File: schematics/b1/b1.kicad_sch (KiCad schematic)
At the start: 7 parts, among them SW6 SW_SPDT, U1 L7805, U8 AMS1117-3.3

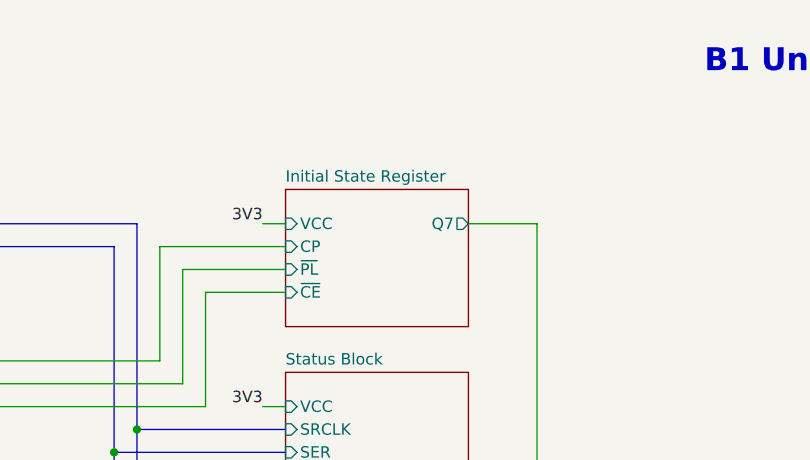
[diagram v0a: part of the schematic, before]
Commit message: Renamed the ISR to the BID Register.
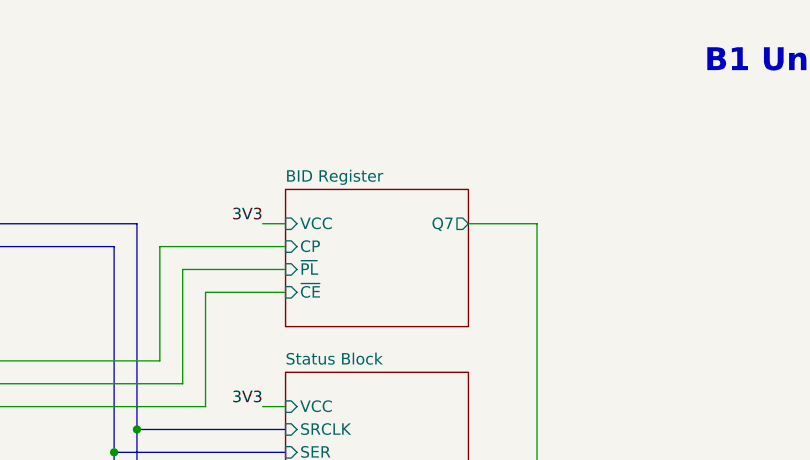
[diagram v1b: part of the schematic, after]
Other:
- sheet Initial State Register renamed BID Register
- sheet BID Register: file initial_state_register.kicad_sch -> bid_register.kicad_sch
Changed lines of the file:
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@@
     (stroke (width 0.1524) (type solid))
     (fill (color 0 0 0 0.0000))
-    (property "Sheetname" "Initial State Register" (at 195.58 31.0384 0)
+    (property "Sheetname" "BID Register" (at 195.58 31.0384 0)
       (effects (font (size 1.27 1.27)) (justify left bottom))
     )
-    (property "Sheetfile" "initial_state_register.kicad_sch" (at 195.58 47.5746 0)
+    (property "Sheetfile" "bid_register.kicad_sch" (at 195.58 47.5746 0)
       (effects (font (size 1.27 1.27)) (justify left top) hide)
     )

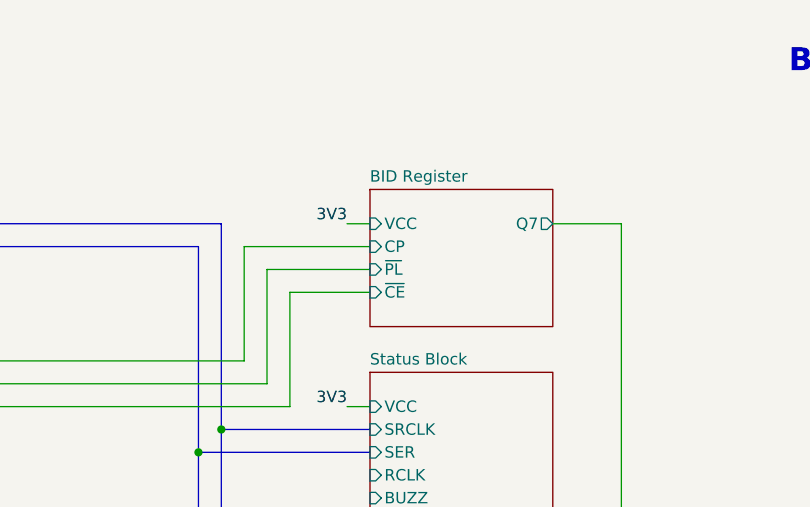
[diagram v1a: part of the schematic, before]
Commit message: Updated the BID register.
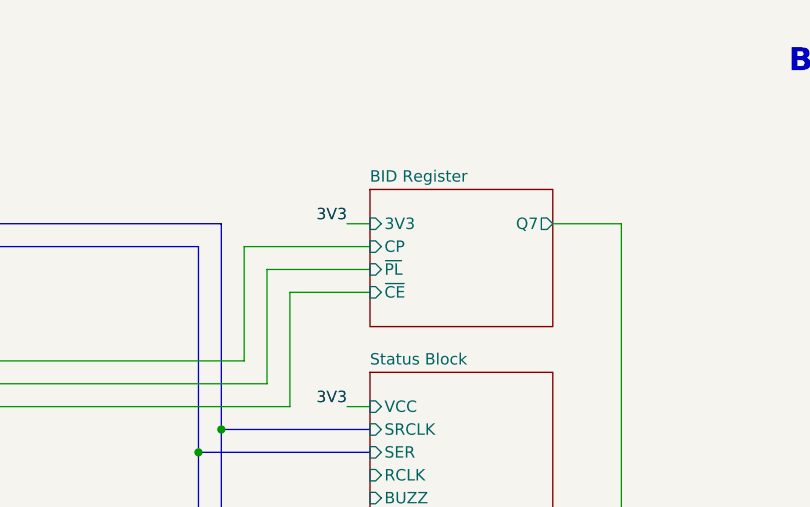
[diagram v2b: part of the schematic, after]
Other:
- sheet BID Register ports: added 3V3; removed VCC
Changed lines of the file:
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@@
       (effects (font (size 1.27 1.27)) (justify right))
-    )
-    (pin "VCC" input (at 195.58 35.56 180)
-      (effects (font (size 1.27 1.27)) (justify left))
     )
     (pin "~{PL}" input (at 195.58 40.64 180)
       (effects (font (size 1.27 1.27)) (justify left))
     )
+    (pin "3V3" input (at 195.58 35.56 180)
+      (effects (font (size 1.27 1.27)) (justify left))
+    )

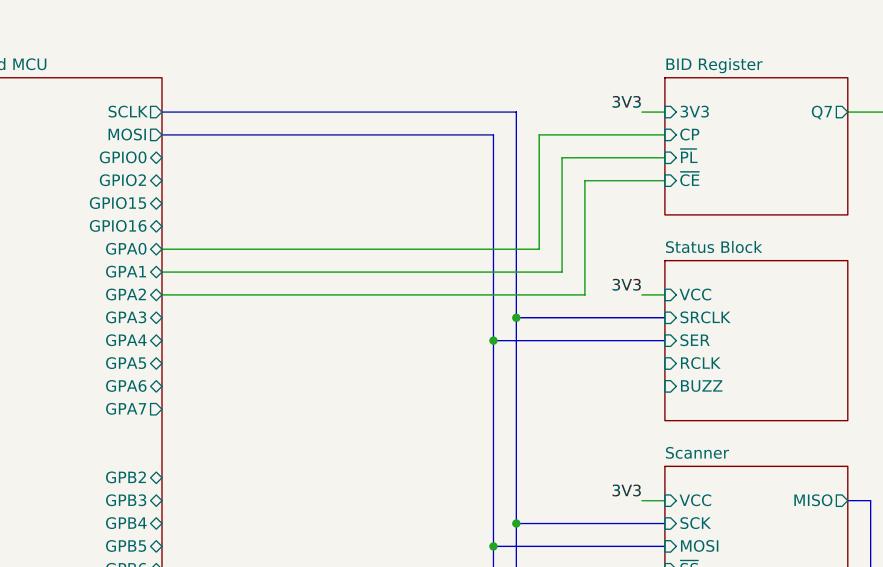
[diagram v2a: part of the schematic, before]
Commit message: Updated status block schematic.
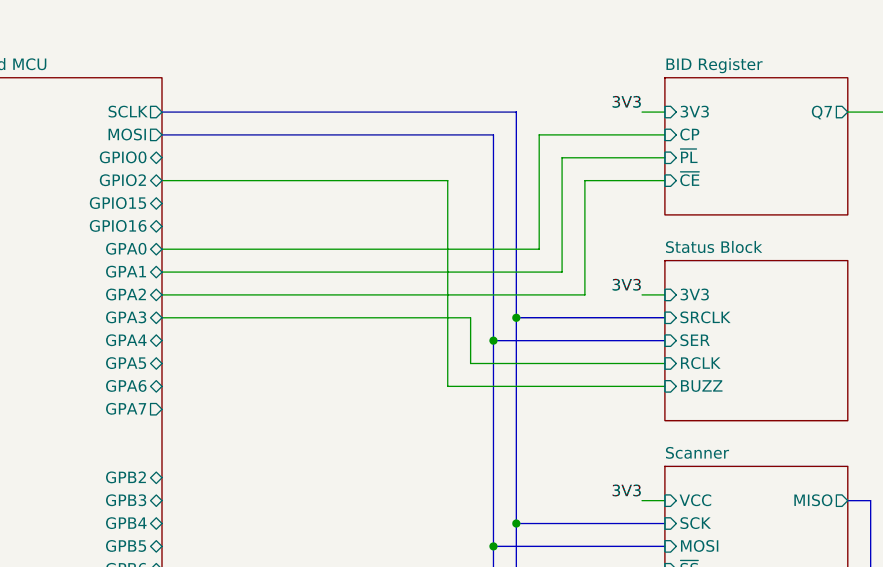
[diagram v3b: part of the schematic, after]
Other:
- sheet Status Block ports: added 3V3; removed VCC
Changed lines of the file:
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@@
+    (stroke (width 0) (type default))
+  )
+  (wire (pts (xy 195.58 63.5) (xy 173.99 63.5))
     (stroke (width 0) (type default))
   )
@@
     (stroke (width 0) (type default))
   )
+  (wire (pts (xy 173.99 63.5) (xy 173.99 58.42))
+    (stroke (width 0) (type default))
+  )
   (wire (pts (xy 184.15 40.64) (xy 184.15 53.34))
     (stroke (width 0) (type default))
@@
     (stroke (width 0) (type default))
   )
+  (wire (pts (xy 171.45 66.04) (xy 171.45 43.18))
+    (stroke (width 0) (type default))
+  )
   (wire (pts (xy 39.37 39.37) (xy 41.91 39.37))
     (stroke (width 0) (type default))
@@
     (stroke (width 0) (type default))
   )
+  (wire (pts (xy 173.99 58.42) (xy 139.7 58.42))
+    (stroke (width 0) (type default))
+  )
   (wire (pts (xy 111.76 35.56) (xy 114.3 35.56))
     (stroke (width 0) (type default))
@@
     (stroke (width 0) (type default))
   )
+  (wire (pts (xy 171.45 43.18) (xy 139.7 43.18))
+    (stroke (width 0) (type default))
+  )
   (bus (pts (xy 195.58 58.42) (xy 179.07 58.42))
     (stroke (width 0) (type default))
@@
   )
   (wire (pts (xy 41.91 69.85) (xy 39.37 69.85))
+    (stroke (width 0) (type default))
+  )
+  (wire (pts (xy 195.58 66.04) (xy 171.45 66.04))
     (stroke (width 0) (type default))
   )
@@
       (effects (font (size 1.27 1.27)) (justify left top) hide)
     )
-    (pin "VCC" input (at 195.58 55.88 180)
-      (effects (font (size 1.27 1.27)) (justify left))
-    )
     (pin "BUZZ" input (at 195.58 66.04 180)
       (effects (font (size 1.27 1.27)) (justify left))
@@
       (effects (font (size 1.27 1.27)) (justify left))
     )
+    (pin "3V3" input (at 195.58 55.88 180)
+      (effects (font (size 1.27 1.27)) (justify left))
+    )

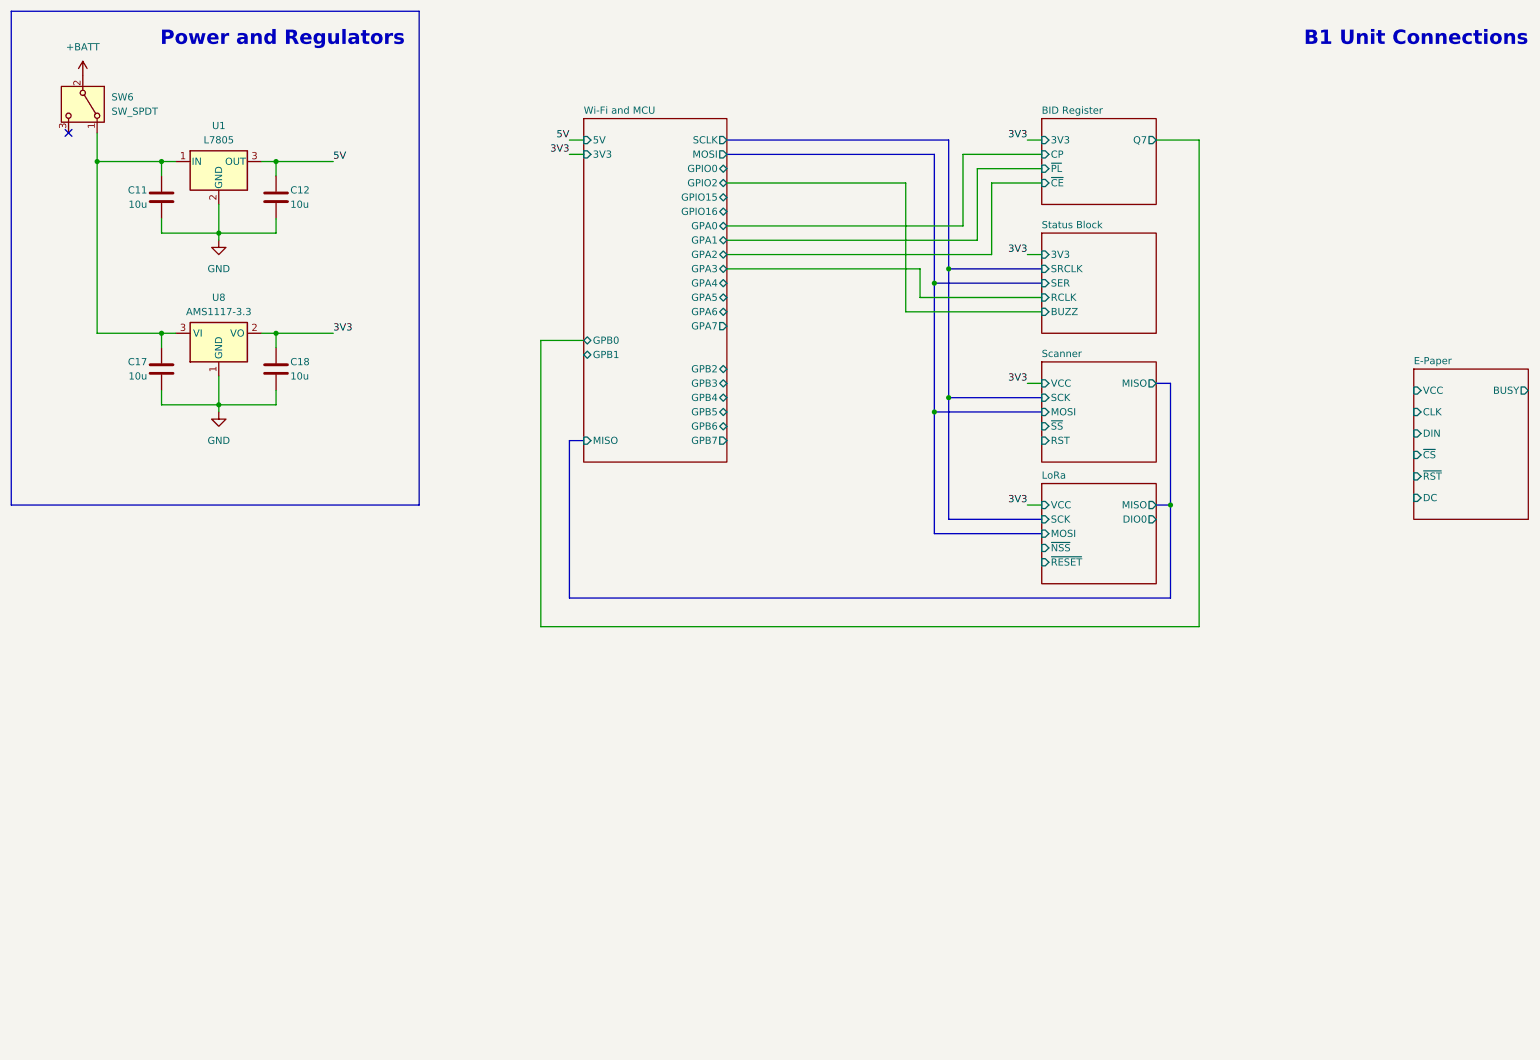
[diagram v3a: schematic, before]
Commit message: Updated RFID scanner wiring.
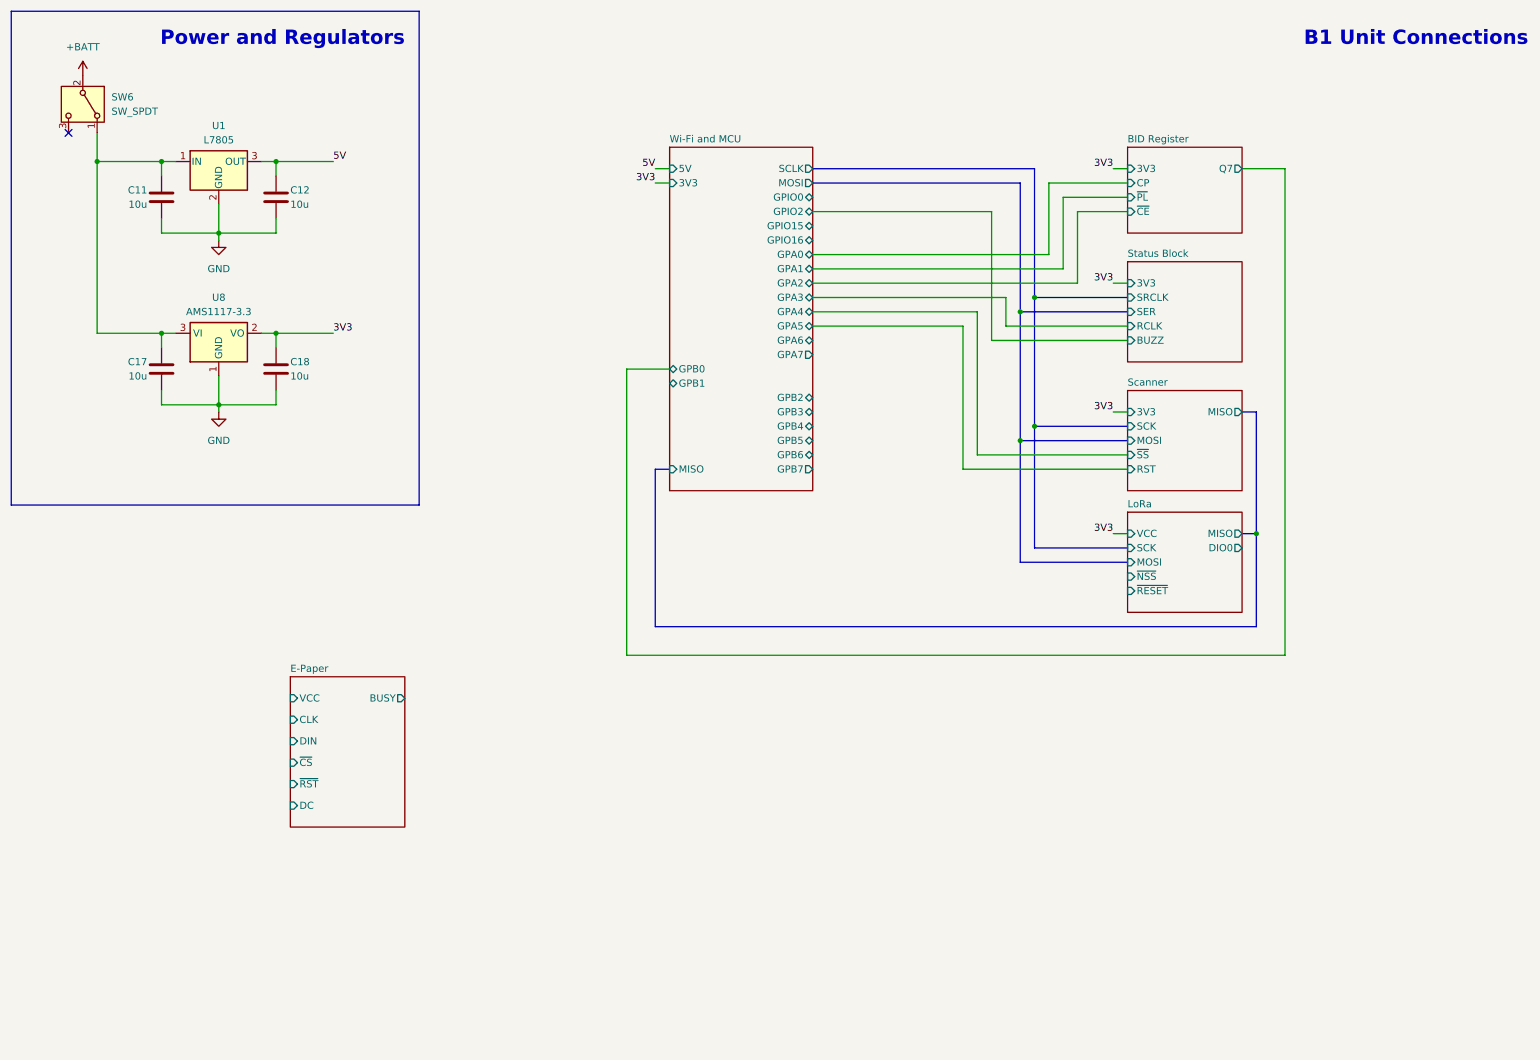
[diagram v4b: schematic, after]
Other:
- sheet Scanner ports: added 3V3; removed VCC

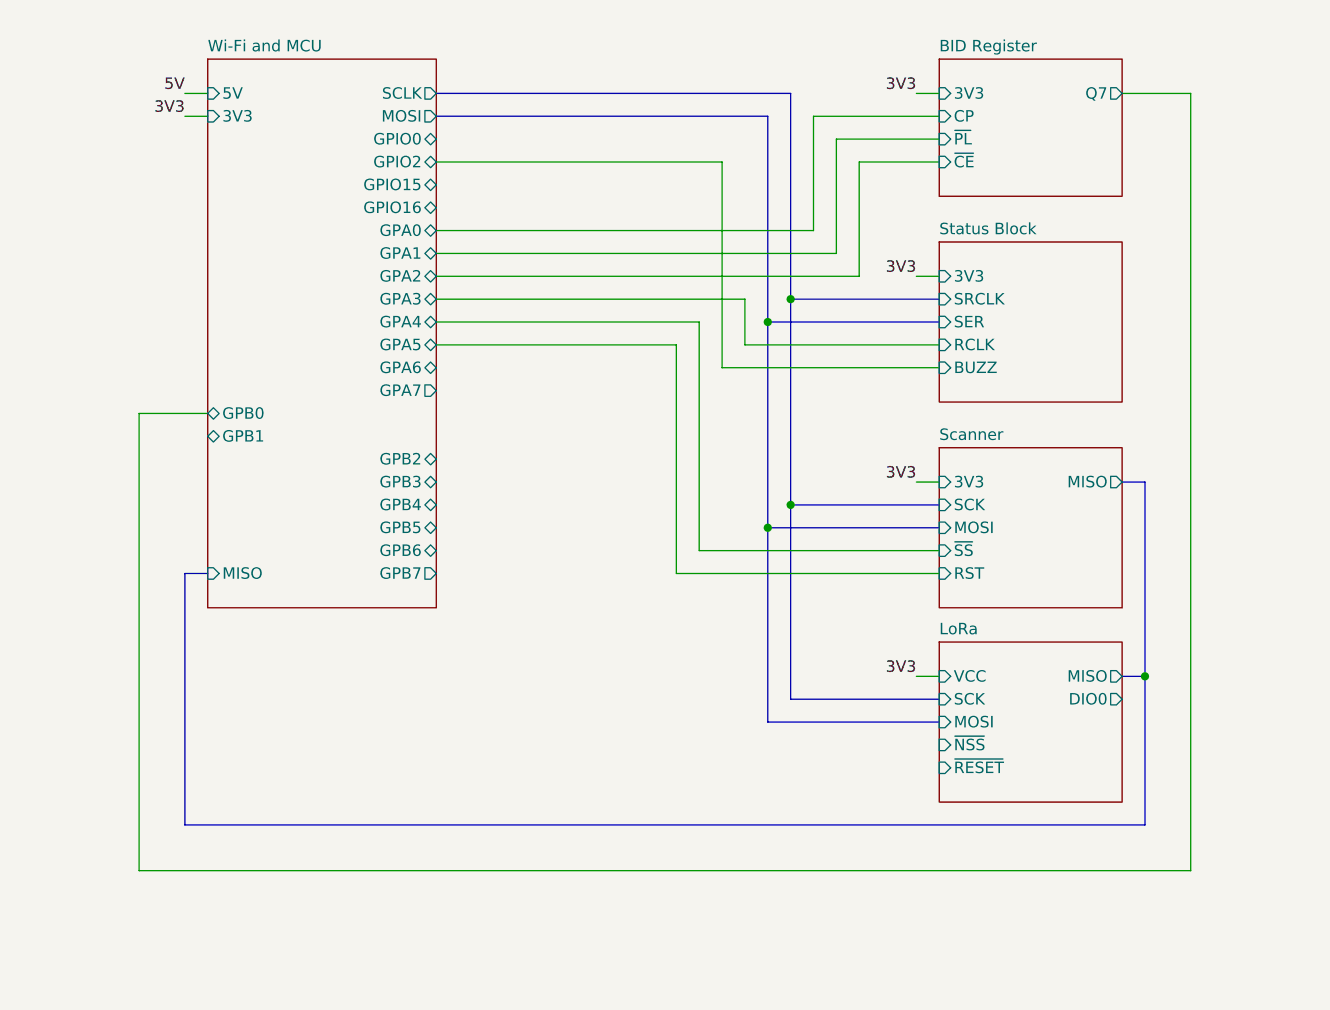
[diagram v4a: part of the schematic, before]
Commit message: Wired LoRa and added a bulk to the status block.
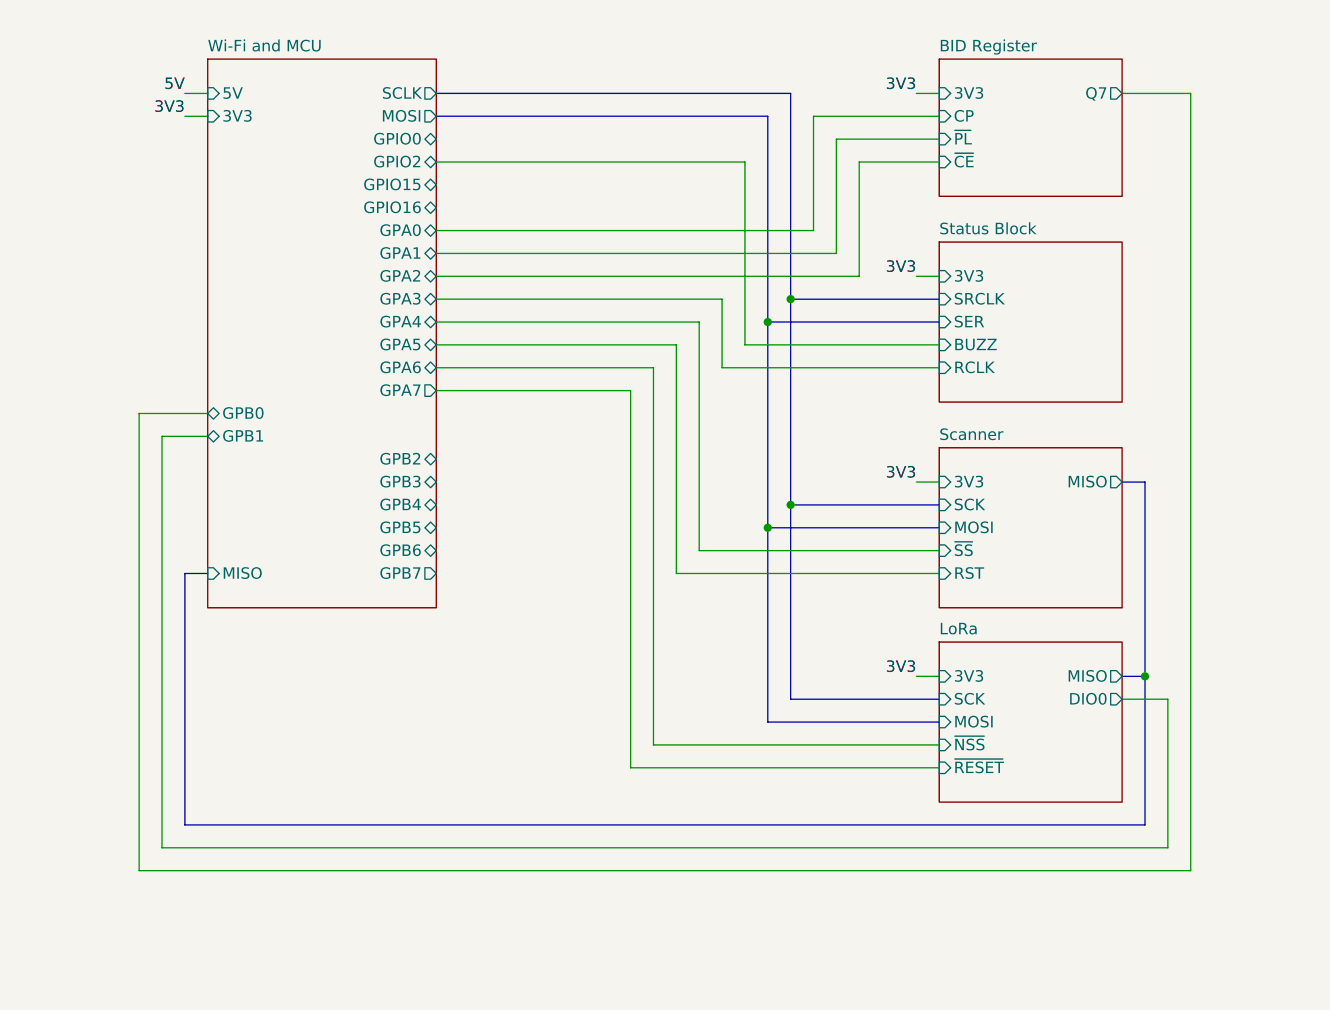
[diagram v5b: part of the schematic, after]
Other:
- sheet LoRa ports: added 3V3; removed VCC
